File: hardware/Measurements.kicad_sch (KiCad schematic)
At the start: 13 parts, among them IC1 MCP1501-10E_SN, IC7 MCP3562T-E_NC, IC9 REF193GSZ-REEL

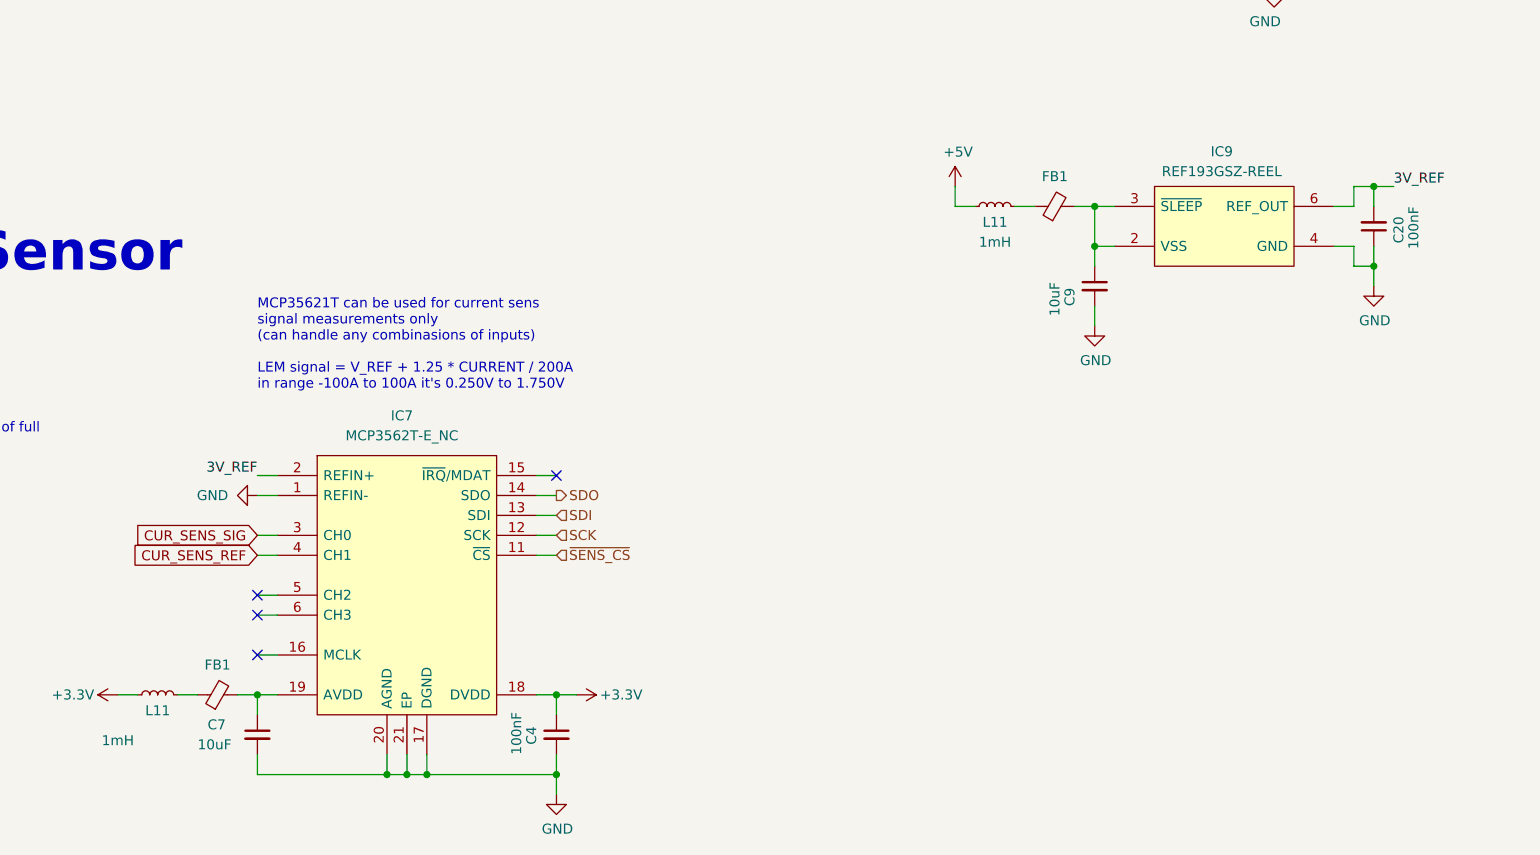
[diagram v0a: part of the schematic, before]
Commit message: symbol update
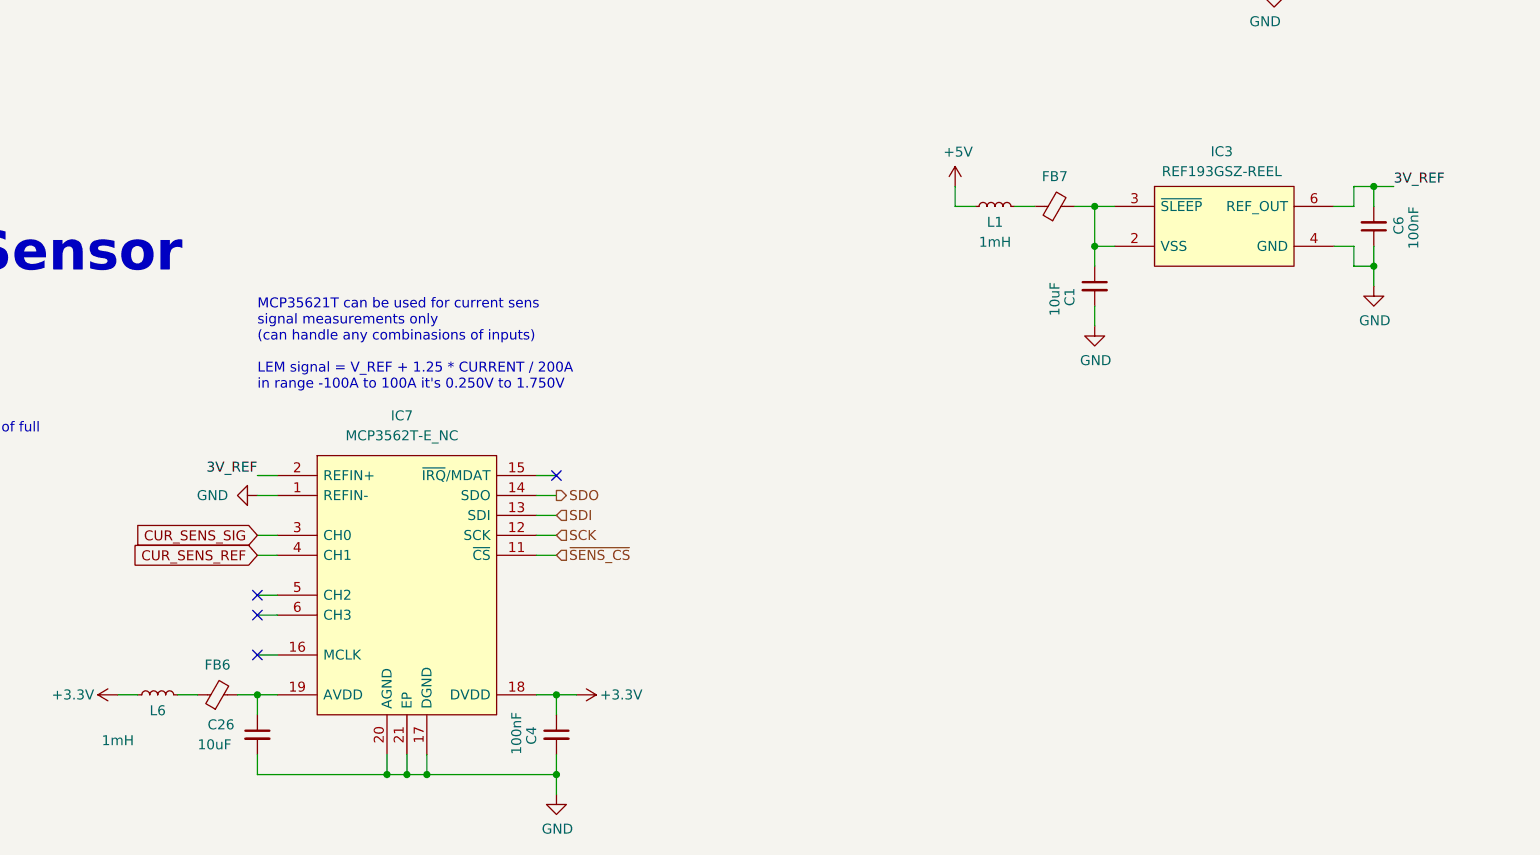
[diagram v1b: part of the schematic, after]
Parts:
- renumbered C9 to C1, C7 to C26, C20 to C6, FB1 to FB6, FB1 to FB7, IC9 to IC3, L11 to L1, L11 to L6
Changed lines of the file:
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@@
   (symbol (lib_id "Device:C_Small") (at 223.52 124.46 0) (unit 1)
     (in_bom yes) (on_board yes) (dnp no)
-    (property "Reference" "C9" (at 220.345 127 90)
+    (property "Reference" "C1" (at 220.345 127 90)
       (effects (font (size 1.27 1.27)) (justify left))
     )
@@
     (instances
       (project "PUTM_EV_BMS_HV_Master_2021"
-        (path "/b456cffc-d9d7-4c91-91f2-36ec9a65dd1b/e61cc821-5479-4c04-b5ab-4a32f17b4f03/d2e30d51-b8f8-4bbd-bb5a-76e0eb119260"
-          (reference "C9") (unit 1)
-        )
-        (path "/b456cffc-d9d7-4c91-91f2-36ec9a65dd1b/e61cc821-5479-4c04-b5ab-4a32f17b4f03/6b03d8c8-5f6c-4244-9202-23821031eb5e"
-          (reference "C46") (unit 1)
-        )
         (path "/b456cffc-d9d7-4c91-91f2-36ec9a65dd1b/e61cc821-5479-4c04-b5ab-4a32f17b4f03"
           (reference "C1") (unit 1)
@@
   (symbol (lib_id "Device:L_Small") (at 104.14 176.53 90) (unit 1)
     (in_bom yes) (on_board yes) (dnp no)
-    (property "Reference" "L11" (at 104.14 177.8 90)
+    (property "Reference" "L6" (at 104.14 177.8 90)
       (effects (font (size 1.27 1.27)) (justify bottom))
     )
@@
     (instances
       (project "PUTM_EV_BMS_HV_Master_2021"
-        (path "/b456cffc-d9d7-4c91-91f2-36ec9a65dd1b/66c3869d-de11-4d8d-b4de-9d98c32ec205"
-          (reference "L11") (unit 1)
-        )
-        (path "/b456cffc-d9d7-4c91-91f2-36ec9a65dd1b/e61cc821-5479-4c04-b5ab-4a32f17b4f03/d2e30d51-b8f8-4bbd-bb5a-76e0eb119260"
-          (reference "L10") (unit 1)
-        )
-        (path "/b456cffc-d9d7-4c91-91f2-36ec9a65dd1b/e61cc821-5479-4c04-b5ab-4a32f17b4f03/6b03d8c8-5f6c-4244-9202-23821031eb5e"
-          (reference "L12") (unit 1)
-        )
         (path "/b456cffc-d9d7-4c91-91f2-36ec9a65dd1b/e61cc821-5479-4c04-b5ab-4a32f17b4f03"
           (reference "L6") (unit 1)
@@
   (symbol (lib_id "Device:Ferrite_Bead_Small") (at 218.44 114.3 90) (unit 1)
     (in_bom yes) (on_board yes) (dnp no)
-    (property "Reference" "FB1" (at 218.44 110.49 90)
+    (property "Reference" "FB7" (at 218.44 110.49 90)
       (effects (font (size 1.27 1.27)))
     )
@@
     (instances
       (project "PUTM_EV_BMS_HV_Master_2021"
-        (path "/b456cffc-d9d7-4c91-91f2-36ec9a65dd1b/66c3869d-de11-4d8d-b4de-9d98c32ec205"
-          (reference "FB1") (unit 1)
-        )
-        (path "/b456cffc-d9d7-4c91-91f2-36ec9a65dd1b/e61cc821-5479-4c04-b5ab-4a32f17b4f03/d2e30d51-b8f8-4bbd-bb5a-76e0eb119260"
-          (reference "FB2") (unit 1)
-        )
-        (path "/b456cffc-d9d7-4c91-91f2-36ec9a65dd1b/e61cc821-5479-4c04-b5ab-4a32f17b4f03/6b03d8c8-5f6c-4244-9202-23821031eb5e"
-          (reference "FB3") (unit 1)
-        )
         (path "/b456cffc-d9d7-4c91-91f2-36ec9a65dd1b/e61cc821-5479-4c04-b5ab-4a32f17b4f03"
           (reference "FB7") (unit 1)
@@
   (symbol (lib_id "Device:Ferrite_Bead_Small") (at 111.76 176.53 90) (unit 1)
     (in_bom yes) (on_board yes) (dnp no)
-    (property "Reference" "FB1" (at 111.76 172.72 90)
+    (property "Reference" "FB6" (at 111.76 172.72 90)
       (effects (font (size 1.27 1.27)))
     )
@@
     (instances
       (project "PUTM_EV_BMS_HV_Master_2021"
-        (path "/b456cffc-d9d7-4c91-91f2-36ec9a65dd1b/66c3869d-de11-4d8d-b4de-9d98c32ec205"
-          (reference "FB1") (unit 1)
-        )
-        (path "/b456cffc-d9d7-4c91-91f2-36ec9a65dd1b/e61cc821-5479-4c04-b5ab-4a32f17b4f03/d2e30d51-b8f8-4bbd-bb5a-76e0eb119260"
-          (reference "FB4") (unit 1)
-        )
-        (path "/b456cffc-d9d7-4c91-91f2-36ec9a65dd1b/e61cc821-5479-4c04-b5ab-4a32f17b4f03/6b03d8c8-5f6c-4244-9202-23821031eb5e"
-          (reference "FB5") (unit 1)
-        )
         (path "/b456cffc-d9d7-4c91-91f2-36ec9a65dd1b/e61cc821-5479-4c04-b5ab-4a32f17b4f03"
           (reference "FB6") (unit 1)
@@
   (symbol (lib_id "Device:C_Small") (at 259.08 116.84 180) (unit 1)
     (in_bom yes) (on_board yes) (dnp no)
-    (property "Reference" "C20" (at 262.255 115.57 90)
+    (property "Reference" "C6" (at 262.255 115.57 90)
       (effects (font (size 1.27 1.27)) (justify left))
     )
@@
     (instances
       (project "PUTM_EV_BMS_HV_Master_2021"
-        (path "/b456cffc-d9d7-4c91-91f2-36ec9a65dd1b/e61cc821-5479-4c04-b5ab-4a32f17b4f03/d2e30d51-b8f8-4bbd-bb5a-76e0eb119260"
-          (reference "C20") (unit 1)
-        )
-        (path "/b456cffc-d9d7-4c91-91f2-36ec9a65dd1b/e61cc821-5479-4c04-b5ab-4a32f17b4f03/6b03d8c8-5f6c-4244-9202-23821031eb5e"
-          (reference "C47") (unit 1)
-        )
         (path "/b456cffc-d9d7-4c91-91f2-36ec9a65dd1b/e61cc821-5479-4c04-b5ab-4a32f17b4f03"
           (reference "C6") (unit 1)
@@
   (symbol (lib_id "Device:L_Small") (at 210.82 114.3 90) (unit 1)
     (in_bom yes) (on_board yes) (dnp no)
-    (property "Reference" "L11" (at 210.82 115.57 90)
+    (property "Reference" "L1" (at 210.82 115.57 90)
       (effects (font (size 1.27 1.27)) (justify bottom))
     )
@@
     (instances
       (project "PUTM_EV_BMS_HV_Master_2021"
-        (path "/b456cffc-d9d7-4c91-91f2-36ec9a65dd1b/66c3869d-de11-4d8d-b4de-9d98c32ec205"
-          (reference "L11") (unit 1)
-        )
-        (path "/b456cffc-d9d7-4c91-91f2-36ec9a65dd1b/e61cc821-5479-4c04-b5ab-4a32f17b4f03/d2e30d51-b8f8-4bbd-bb5a-76e0eb119260"
-          (reference "L2") (unit 1)
-        )
-        (path "/b456cffc-d9d7-4c91-91f2-36ec9a65dd1b/e61cc821-5479-4c04-b5ab-4a32f17b4f03/6b03d8c8-5f6c-4244-9202-23821031eb5e"
-          (reference "L7") (unit 1)
-        )
         (path "/b456cffc-d9d7-4c91-91f2-36ec9a65dd1b/e61cc821-5479-4c04-b5ab-4a32f17b4f03"
           (reference "L1") (unit 1)
@@
   (symbol (lib_id "Device:C_Small") (at 116.84 181.61 0) (unit 1)
     (in_bom yes) (on_board yes) (dnp no)
-    (property "Reference" "C7" (at 110.49 180.34 0)
+    (property "Reference" "C26" (at 110.49 180.34 0)
       (effects (font (size 1.27 1.27)) (justify left))
     )
@@
     (instances
       (project "PUTM_EV_BMS_HV_Master_2021"
-        (path "/b456cffc-d9d7-4c91-91f2-36ec9a65dd1b/e61cc821-5479-4c04-b5ab-4a32f17b4f03/d2e30d51-b8f8-4bbd-bb5a-76e0eb119260"
-          (reference "C7") (unit 1)
-        )
-        (path "/b456cffc-d9d7-4c91-91f2-36ec9a65dd1b/e61cc821-5479-4c04-b5ab-4a32f17b4f03/6b03d8c8-5f6c-4244-9202-23821031eb5e"
-          (reference "C22") (unit 1)
-        )
         (path "/b456cffc-d9d7-4c91-91f2-36ec9a65dd1b/e61cc821-5479-4c04-b5ab-4a32f17b4f03"
           (reference "C26") (unit 1)
@@
   (symbol (lib_id "power:+5V") (at 205.74 111.76 0) (unit 1)
     (in_bom yes) (on_board yes) (dnp no)
-    (property "Reference" "#PWR087" (at 205.74 115.57 0)
+    (property "Reference" "#PWR0104" (at 205.74 115.57 0)
       (effects (font (size 1.27 1.27)) hide)
     )
@@
     (instances
       (project "PUTM_EV_BMS_HV_Master_2021"
-        (path "/b456cffc-d9d7-4c91-91f2-36ec9a65dd1b/66c3869d-de11-4d8d-b4de-9d98c32ec205"
-          (reference "#PWR087") (unit 1)
-        )
         (path "/b456cffc-d9d7-4c91-91f2-36ec9a65dd1b/e61cc821-5479-4c04-b5ab-4a32f17b4f03"
           (reference "#PWR0104") (unit 1)
@@
   (symbol (lib_id "REF196GSZ-REEL:REF196GSZ-REEL") (at 240.03 116.84 0) (unit 1)
     (in_bom yes) (on_board yes) (dnp no) (fields_autoplaced)
-    (property "Reference" "IC9" (at 239.7125 107.315 0)
+    (property "Reference" "IC3" (at 239.7125 107.315 0)
       (effects (font (size 1.27 1.27)))
     )
@@
     (instances
       (project "PUTM_EV_BMS_HV_Master_2021"
-        (path "/b456cffc-d9d7-4c91-91f2-36ec9a65dd1b/e61cc821-5479-4c04-b5ab-4a32f17b4f03/d2e30d51-b8f8-4bbd-bb5a-76e0eb119260"
-          (reference "IC9") (unit 1)
-        )
-        (path "/b456cffc-d9d7-4c91-91f2-36ec9a65dd1b/e61cc821-5479-4c04-b5ab-4a32f17b4f03/6b03d8c8-5f6c-4244-9202-23821031eb5e"
-          (reference "IC10") (unit 1)
-        )
         (path "/b456cffc-d9d7-4c91-91f2-36ec9a65dd1b/e61cc821-5479-4c04-b5ab-4a32f17b4f03"
           (reference "IC3") (unit 1)

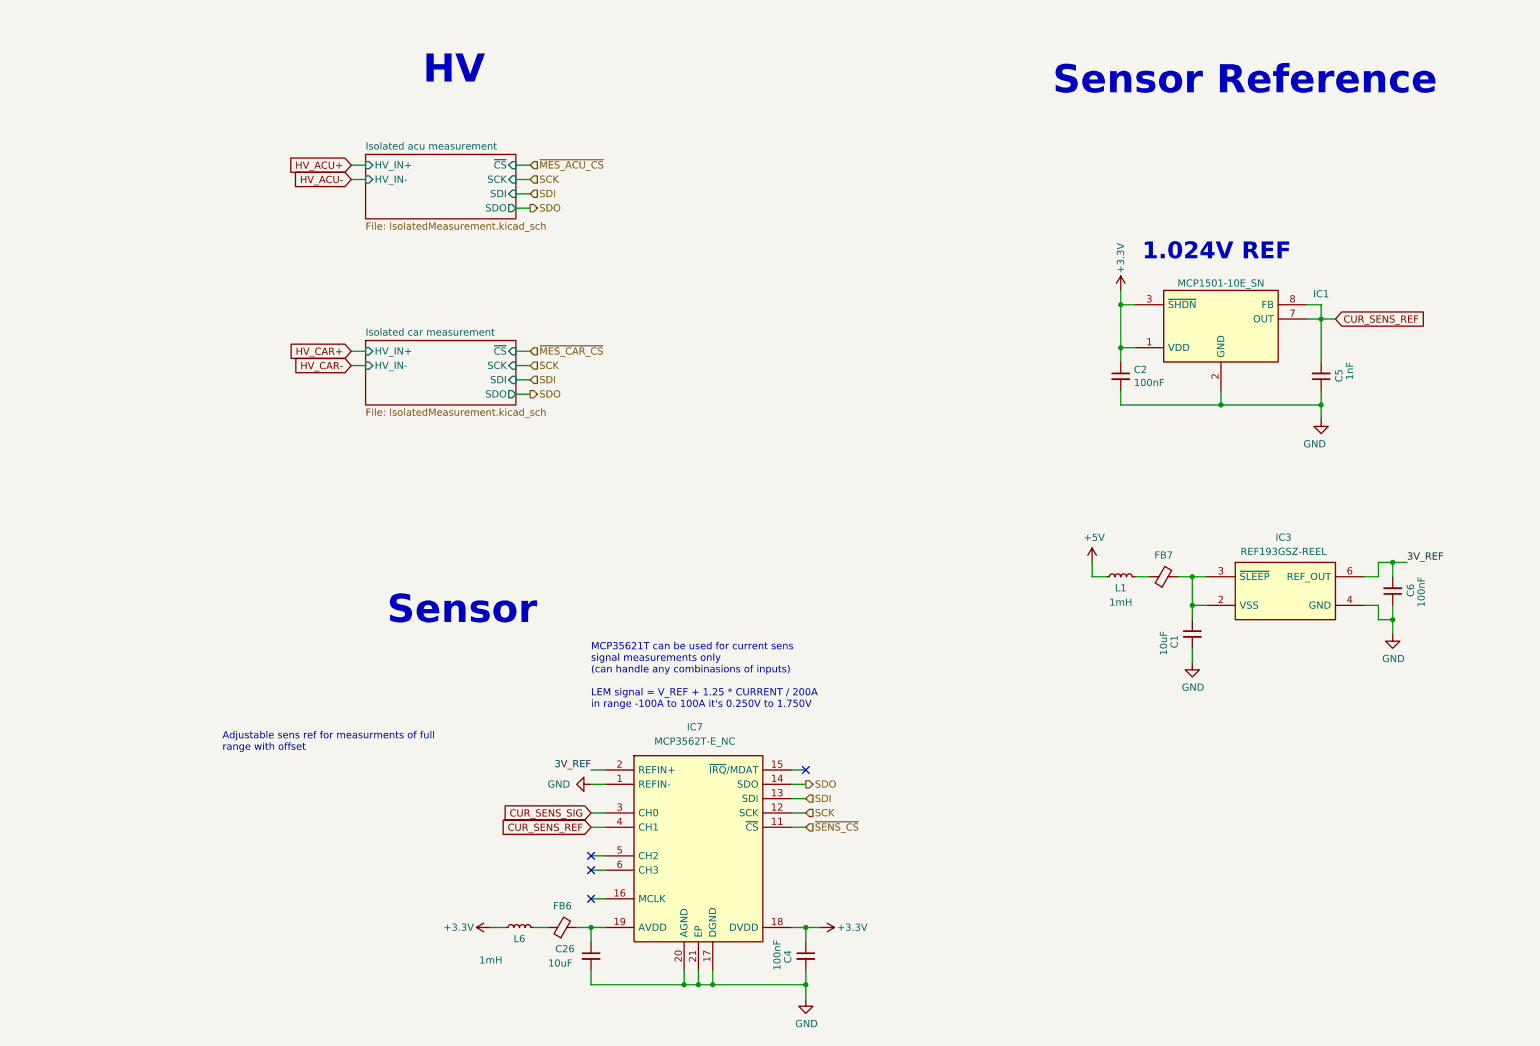
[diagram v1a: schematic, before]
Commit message: schematic clean up
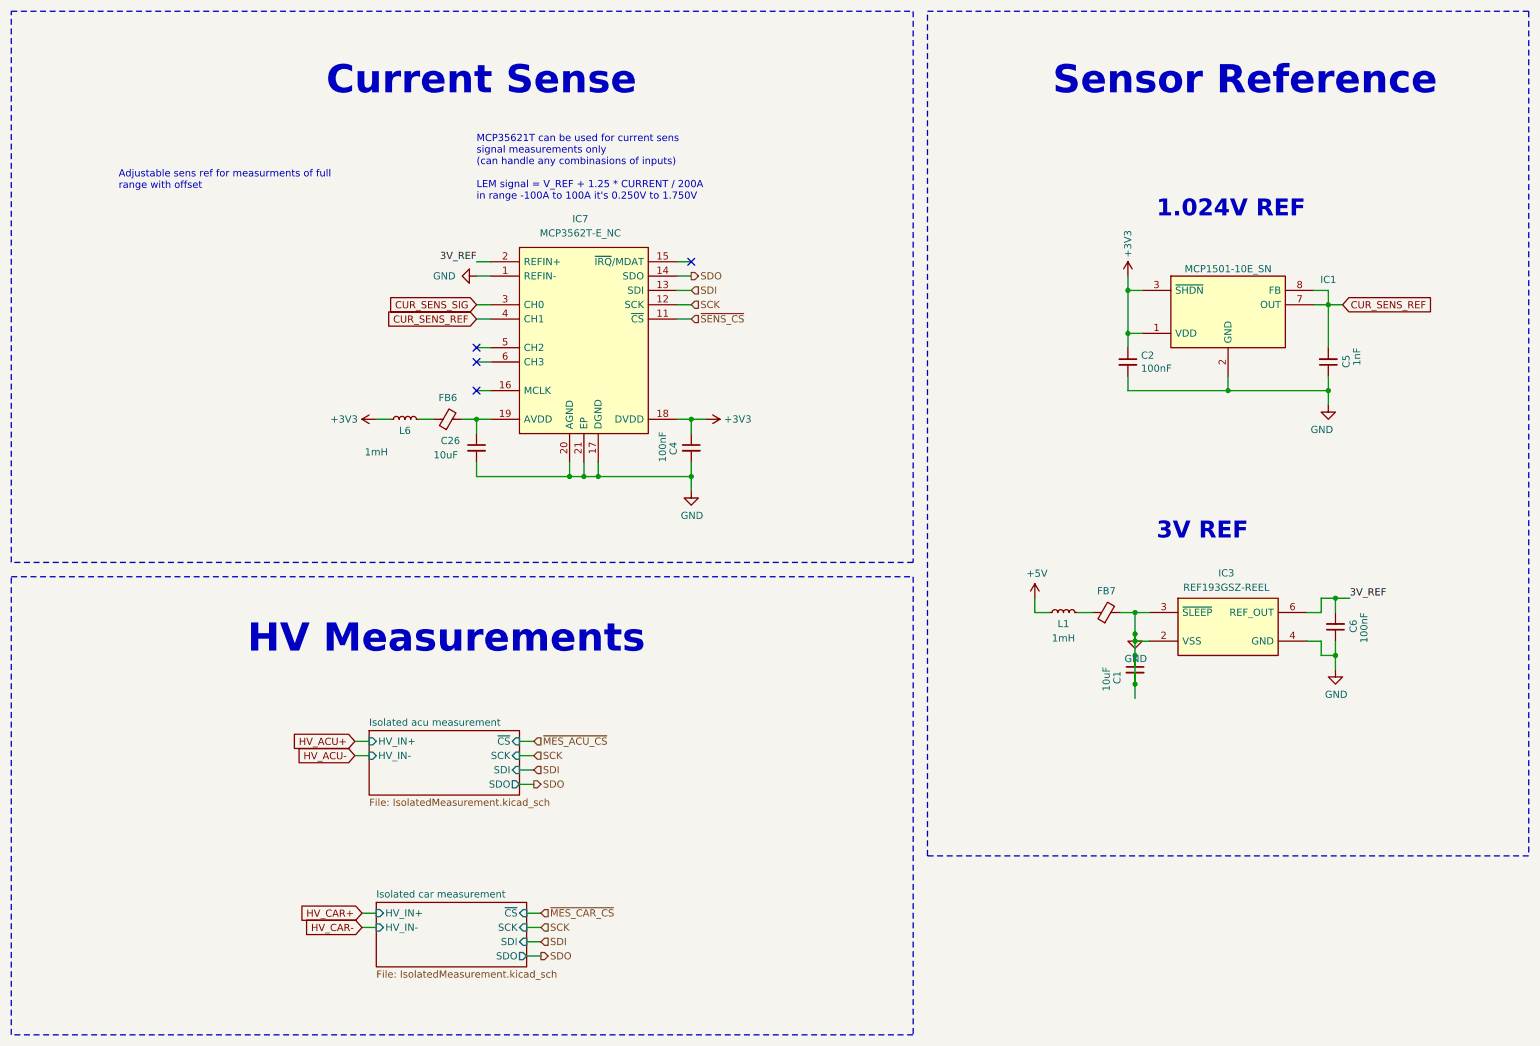
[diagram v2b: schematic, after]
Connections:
- net GND: now also C1.1, FB7.2, IC3.2 (VSS), IC3.3 (~{SLEEP})
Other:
- note added: "3V REF"
- note added: "Current Sense"
- note added: "HV Measurements"
- note removed: "HV"
- note removed: "Sensor"
- moved on the sheet: C1, C2, C26, C4, C5, C6, FB6, FB7, IC1, IC3, IC7, L1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
